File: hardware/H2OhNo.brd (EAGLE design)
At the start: 43.2 x 43.2 mm, 15 parts, among them U2 Tiny85-20-SMT

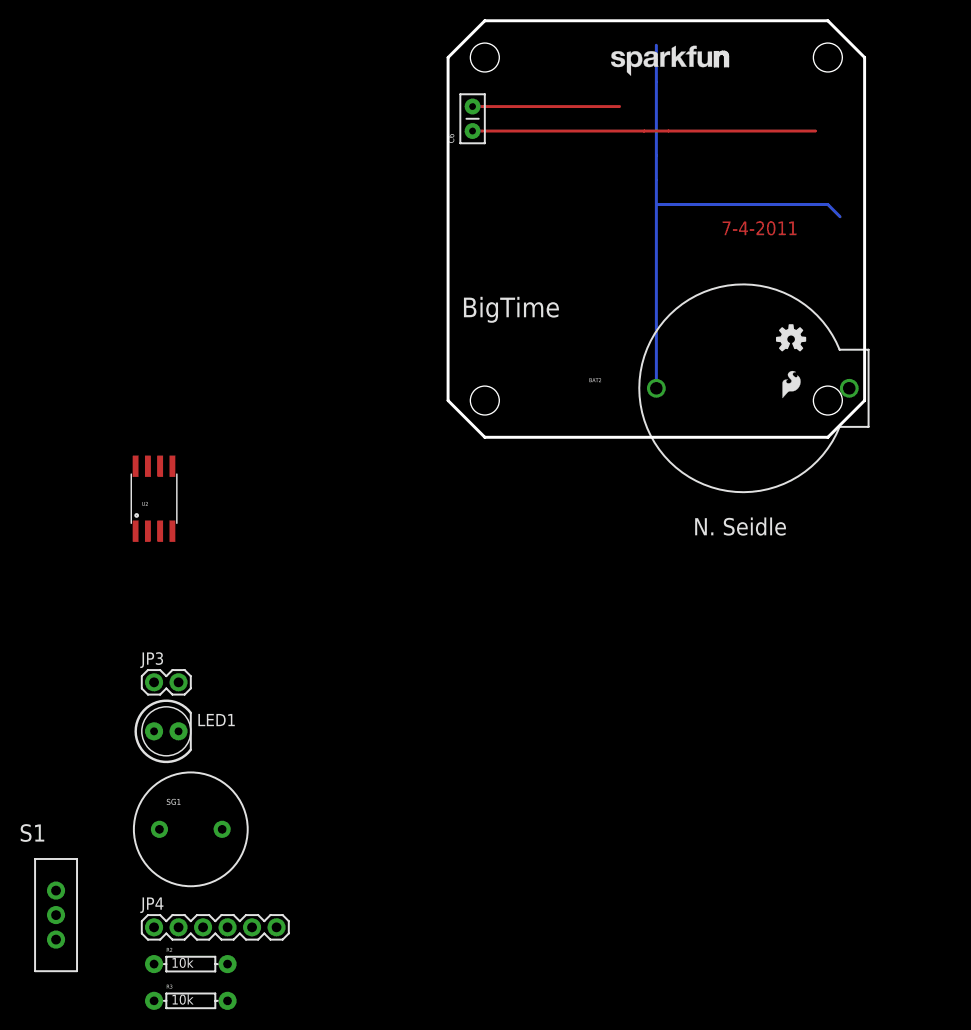
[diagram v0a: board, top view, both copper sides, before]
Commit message: Added version #. Fixed file naming. Removed 10k on RES.
Fixed footprint on CR2032 as well.
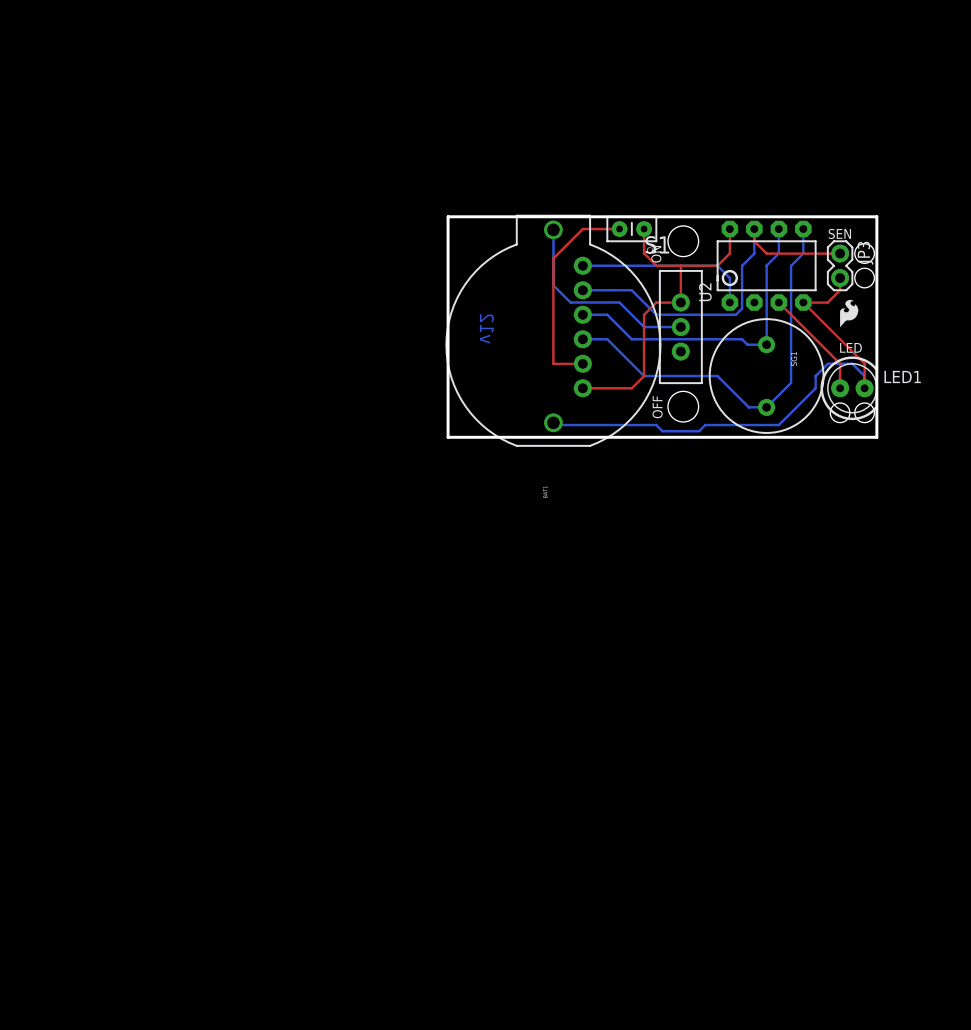
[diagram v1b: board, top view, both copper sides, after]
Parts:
- removed BAT2: (no value), Testing:BATTCOM_20MM_PTH
- removed R2, R3: 10k, SparkFun:AXIAL-0.3
- removed U$3: LOGO-SFENEW, SparkFun:SFE-NEW-WEBLOGO
- added BAT1: (no value), SparkFun-Electromechanical:BATTCOM_20MM_PTH
- U2: value Tiny85-20-SMT -> TINY85-20-DIP; device SparkFun-DigitalIC:SO08-EIAJ -> SparkFun-DigitalIC:DIP08
- moved S1 88.9 mm to (24.1, 11.4)
- moved JP3 83.9 mm to (40.6, 19.1), turned to 270 degrees
- moved JP4 81.7 mm to (14.0, 17.8), flipped to the bottom, turned to 270 degrees
- moved LED1 79.5 mm to (41.9, 5.08)
- moved SG1 76.0 mm to (33.0, 6.35), turned to 270 degrees
- moved U2 67.9 mm to (33.0, 17.8)
- moved U$5 34.3 mm to (4.95, 5.33), flipped to the bottom, turned to 90 degrees
- moved C6 20.5 mm to (20.3, 21.6), turned to 180 degrees
- moved U$4 15.3 mm to (20.3, 11.4), flipped to the bottom, turned to 90 degrees
- moved U$1 9.48 mm to (40.6, 11.4)
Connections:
- removed net N$5: LED1.K, R3.P$2
- net D1: now also SG1.-; no longer LED1.A
- net D4: now also LED1.A
- net GND: now also BAT1.2, LED1.K; no longer BAT2.2, R3.P$1, SG1.-
- net N$1: now also BAT1.1; no longer BAT2.1
- net RESET: no longer R2.P$1
- net VCC: no longer R2.P$2
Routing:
- net D0: track 0.00 -> 42.0 mm
- net D2: track 0.00 -> 37.3 mm
- net D1: track 0.00 -> 32.9 mm
- net N$1: track 0.00 -> 20.8 mm
- net RESET: track 0.00 -> 18.3 mm
- net D4: track 0.00 -> 11.5 mm
- net GND: track 70.4 -> 77.0 mm, vias 1 -> 0
- net VCC: track 35.6 -> 36.4 mm
- added copper zone on layer 1, net GND
- added copper zone on layer 16, net GND
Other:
- board size 43.2 x 43.2 mm -> 44.5 x 22.9 mm
- board text added: "H2OhNo!"
- board text added: "ISP"
- board text added: "LED"
- board text added: "OFF"
- board text added: "ON"
- board text added: "RST"
- board text added: "SEN"
- board text added: "VCC"
- board text added: "v12"
- board text removed: "7-4-2011"
- board text removed: "BLK"
- board text removed: "BigTime"
- board text removed: "Built on:"
- board text removed: "FTDI"
- board text removed: "GRN"

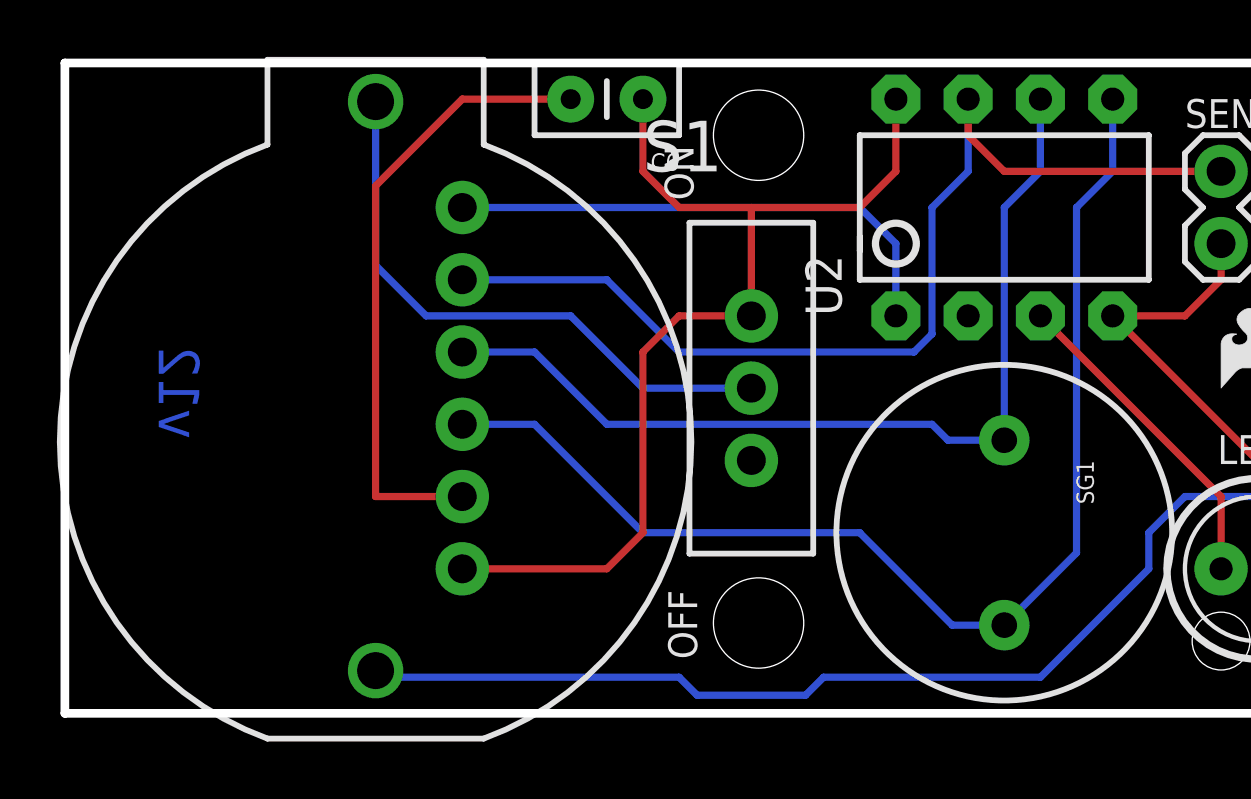
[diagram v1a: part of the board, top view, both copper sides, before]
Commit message: Modified 6-pin SIP header for FTDI compatibility
It's not serial, but you should be able to bit-bang serial out the
MOSI/MISO lines and use an FTDI on the programming header. Good for
debugging.
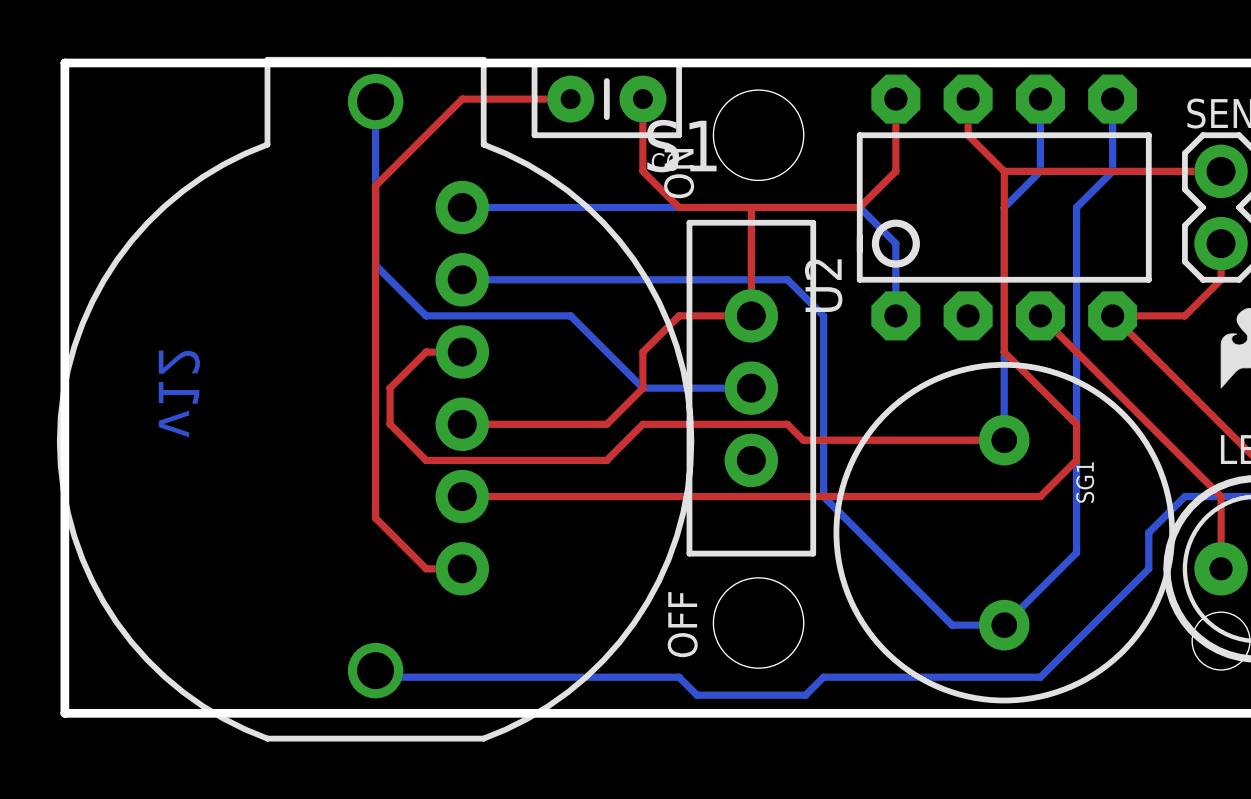
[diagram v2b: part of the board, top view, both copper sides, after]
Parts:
- JP3: value Sense -> Water Sensor
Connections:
- net D0: now also JP4.2; no longer JP4.4
- net D2: now also JP4.5; no longer JP4.2
- net GND: now also JP4.6; no longer JP4.5
- net VCC: now also JP4.4; no longer JP4.6
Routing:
- net D1: track 32.9 -> 39.7 mm
- net D2: track 37.3 -> 44.0 mm
- net D0: track 42.0 -> 47.9 mm
- net VCC: track 36.4 -> 31.3 mm
- net GND: track 77.0 -> 78.5 mm
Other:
- board text added: "GND"
- board text removed: "VCC"
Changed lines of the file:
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@@
 <layer number="106" name="bPlate" color="7" fill="1" visible="no" active="yes"/>
 <layer number="107" name="Crop" color="7" fill="1" visible="no" active="yes"/>
-<layer number="108" name="tplace-old" color="10" fill="1" visible="yes" active="yes"/>
-<layer number="109" name="ref-old" color="11" fill="1" visible="yes" active="yes"/>
+<layer number="108" name="tplace-old" color="10" fill="1" visible="no" active="yes"/>
+<layer number="109" name="ref-old" color="11" fill="1" visible="no" active="yes"/>
 <layer number="116" name="Patch_BOT" color="9" fill="4" visible="no" active="yes"/>
 <layer number="121" name="_tsilk" color="7" fill="1" visible="no" active="yes"/>
@@
 <wire x1="44.45" y1="22.86" x2="0" y2="22.86" width="0.3048" layer="20"/>
 <text x="0.635" y="5.715" size="2.032" layer="22" font="vector" ratio="15" rot="MR90">H2OhNo!</text>
-<text x="3.302" y="9.652" size="1.4224" layer="16" font="vector" ratio="15" rot="SMR90">v12</text>
+<text x="3.302" y="9.652" size="1.4224" layer="16" font="vector" ratio="20" rot="SMR90">v12</text>
 <text x="25.4" y="-10.16" size="1.778" layer="48" font="vector" ratio="15">N. Seidle</text>
 <text x="11.43" y="16.51" size="1.016" layer="22" font="vector" ratio="15" rot="MR90">RST</text>
-<text x="11.43" y="3.81" size="1.016" layer="22" font="vector" ratio="15" rot="MR90">VCC</text>
+<text x="11.43" y="3.81" size="1.016" layer="22" font="vector" ratio="15" rot="MR90">GND</text>
 <text x="10.033" y="9.906" size="1.016" layer="22" font="vector" ratio="15" rot="MR90">ISP</text>
 <hole x="24.384" y="20.32" drill="3.175"/>
@@
 <attribute name="VALUE" value="TINY85-20-DIP" x="33.02" y="17.78" size="1.778" layer="27" font="vector" ratio="15" display="off"/>
 </element>
-<element name="JP3" library="SparkFun-Connectors" package="1X02" value="Sense" x="40.64" y="19.05" rot="R270"/>
+<element name="JP3" library="SparkFun-Connectors" package="1X02" value="Water Sensor" x="40.64" y="19.05" rot="R270"/>
 <element name="LED1" library="SparkFun-LED" package="LED5MM" value="" x="41.91" y="5.08"/>
 <element name="SG1" library="SparkFun-Electromechanical" package="BUZZER-12MM" value="BUZZERPTH" x="33.02" y="6.35" rot="R270"/>
@@
 <signal name="GND">
 <contactref element="C6" pad="2"/>
-<contactref element="JP4" pad="5"/>
 <contactref element="U2" pad="4"/>
 <contactref element="JP3" pad="2"/>
@@
 <wire x1="40.64" y1="15.24" x2="40.64" y2="16.51" width="0.254" layer="1"/>
 <wire x1="17.78" y1="21.59" x2="13.97" y2="21.59" width="0.254" layer="1"/>
-<wire x1="13.97" y1="7.62" x2="10.922" y2="7.62" width="0.254" layer="1"/>
 <wire x1="43.18" y1="5.08" x2="43.18" y2="6.35" width="0.254" layer="16"/>
 <wire x1="43.18" y1="6.35" x2="41.91" y2="7.62" width="0.254" layer="16"/>
@@
 <wire x1="38.1" y1="5.08" x2="34.29" y2="1.27" width="0.254" layer="16"/>
 <wire x1="43.18" y1="7.62" x2="43.18" y2="5.08" width="0.254" layer="1"/>
-<wire x1="10.922" y1="7.62" x2="10.922" y2="18.542" width="0.254" layer="1"/>
+<wire x1="10.922" y1="6.858" x2="10.922" y2="18.542" width="0.254" layer="1"/>
 <wire x1="10.922" y1="18.542" x2="13.97" y2="21.59" width="0.254" layer="1"/>
 <wire x1="34.29" y1="1.27" x2="26.67" y2="1.27" width="0.254" layer="16"/>
@@
 </polygon>
 <contactref element="BAT1" pad="2"/>
+<contactref element="JP4" pad="6"/>
+<wire x1="10.922" y1="6.858" x2="12.7" y2="5.08" width="0.254" layer="1"/>
+<wire x1="12.7" y1="5.08" x2="13.97" y2="5.08" width="0.254" layer="1"/>
 </signal>
 <signal name="VCC">
 <contactref element="C6" pad="1"/>
-<contactref element="JP4" pad="6"/>
 <contactref element="U2" pad="8"/>
 <contactref element="S1" pad="1"/>
-<wire x1="20.32" y1="12.7" x2="20.32" y2="6.35" width="0.254" layer="1"/>
-<wire x1="20.32" y1="6.35" x2="19.05" y2="5.08" width="0.254" layer="1"/>
-<wire x1="19.05" y1="5.08" x2="13.97" y2="5.08" width="0.254" layer="1"/>
 <wire x1="24.13" y1="17.78" x2="27.94" y2="17.78" width="0.254" layer="1"/>
 <wire x1="24.13" y1="13.97" x2="24.13" y2="17.78" width="0.254" layer="1"/>
@@
 <wire x1="27.94" y1="17.78" x2="29.21" y2="19.05" width="0.254" layer="1"/>
 <wire x1="29.21" y1="19.05" x2="29.21" y2="21.59" width="0.254" layer="1"/>
+<contactref element="JP4" pad="4"/>
+<wire x1="13.97" y1="10.16" x2="19.05" y2="10.16" width="0.254" layer="1"/>
+<wire x1="19.05" y1="10.16" x2="20.32" y2="11.43" width="0.254" layer="1"/>
+<wire x1="20.32" y1="11.43" x2="20.32" y2="12.7" width="0.254" layer="1"/>
 </signal>
 <signal name="RESET">
@@
 </signal>
 <signal name="D0">
-<contactref element="JP4" pad="4"/>
 <contactref element="U2" pad="5"/>
 <contactref element="SG1" pad="+"/>
@@
 <wire x1="35.56" y1="5.64" x2="33.02" y2="3.1" width="0.254" layer="16"/>
 <wire x1="33.02" y1="3.1" x2="31.19" y2="3.1" width="0.254" layer="16"/>
-<wire x1="31.19" y1="3.1" x2="27.94" y2="6.35" width="0.254" layer="16"/>
-<wire x1="27.94" y1="6.35" x2="20.32" y2="6.35" width="0.254" layer="16"/>
-<wire x1="20.32" y1="6.35" x2="16.51" y2="10.16" width="0.254" layer="16"/>
-<wire x1="16.51" y1="10.16" x2="13.97" y2="10.16" width="0.254" layer="16"/>
+<wire x1="31.19" y1="3.1" x2="26.67" y2="7.62" width="0.254" layer="16"/>
+<contactref element="JP4" pad="2"/>
+<wire x1="13.97" y1="15.24" x2="25.4" y2="15.24" width="0.254" layer="16"/>
+<wire x1="25.4" y1="15.24" x2="26.67" y2="13.97" width="0.254" layer="16"/>
+<wire x1="26.67" y1="13.97" x2="26.67" y2="7.62" width="0.254" layer="16"/>
 </signal>
 <signal name="D1">
-<contactref element="JP4" pad="3"/>
 <contactref element="U2" pad="6"/>
 <contactref element="SG1" pad="-"/>
-<wire x1="13.97" y1="12.7" x2="16.51" y2="12.7" width="0.254" layer="16"/>
-<wire x1="16.51" y1="12.7" x2="19.05" y2="10.16" width="0.254" layer="16"/>
-<wire x1="33.02" y1="9.6" x2="31.04" y2="9.6" width="0.254" layer="16"/>
-<wire x1="31.04" y1="9.6" x2="30.48" y2="10.16" width="0.254" layer="16"/>
-<wire x1="30.48" y1="10.16" x2="19.05" y2="10.16" width="0.254" layer="16"/>
 <wire x1="34.29" y1="21.59" x2="34.29" y2="19.05" width="0.254" layer="16"/>
 <wire x1="34.29" y1="19.05" x2="33.02" y2="17.78" width="0.254" layer="16"/>
 <wire x1="33.02" y1="17.78" x2="33.02" y2="9.6" width="0.254" layer="16"/>
+<contactref element="JP4" pad="3"/>
+<wire x1="33.02" y1="9.6" x2="25.96" y2="9.6" width="0.254" layer="1"/>
+<wire x1="25.96" y1="9.6" x2="25.4" y2="10.16" width="0.254" layer="1"/>
+<wire x1="25.4" y1="10.16" x2="20.32" y2="10.16" width="0.254" layer="1"/>
+<wire x1="20.32" y1="10.16" x2="19.05" y2="8.89" width="0.254" layer="1"/>
+<wire x1="19.05" y1="8.89" x2="12.7" y2="8.89" width="0.254" layer="1"/>
+<wire x1="12.7" y1="8.89" x2="11.43" y2="10.16" width="0.254" layer="1"/>
+<wire x1="11.43" y1="10.16" x2="11.43" y2="11.43" width="0.254" layer="1"/>
+<wire x1="11.43" y1="11.43" x2="12.7" y2="12.7" width="0.254" layer="1"/>
+<wire x1="12.7" y1="12.7" x2="13.97" y2="12.7" width="0.254" layer="1"/>
 </signal>
 <signal name="D2">
-<contactref element="JP4" pad="2"/>
 <contactref element="U2" pad="7"/>
 <contactref element="JP3" pad="1"/>
-<wire x1="13.97" y1="15.24" x2="19.05" y2="15.24" width="0.254" layer="16"/>
-<wire x1="19.05" y1="15.24" x2="21.59" y2="12.7" width="0.254" layer="16"/>
-<wire x1="21.59" y1="12.7" x2="29.845" y2="12.7" width="0.254" layer="16"/>
-<wire x1="29.845" y1="12.7" x2="30.48" y2="13.335" width="0.254" layer="16"/>
 <wire x1="40.64" y1="19.05" x2="33.02" y2="19.05" width="0.254" layer="1"/>
-<wire x1="30.48" y1="13.335" x2="30.48" y2="17.78" width="0.254" layer="16"/>
-<wire x1="30.48" y1="17.78" x2="31.75" y2="19.05" width="0.254" layer="16"/>
-<wire x1="31.75" y1="19.05" x2="31.75" y2="21.59" width="0.254" layer="16"/>
+<contactref element="JP4" pad="5"/>
+<wire x1="13.97" y1="7.62" x2="34.29" y2="7.62" width="0.254" layer="1"/>
+<wire x1="34.29" y1="7.62" x2="35.56" y2="8.89" width="0.254" layer="1"/>
+<wire x1="35.56" y1="8.89" x2="35.56" y2="10.16" width="0.254" layer="1"/>
+<wire x1="35.56" y1="10.16" x2="33.02" y2="12.7" width="0.254" layer="1"/>
+<wire x1="33.02" y1="12.7" x2="33.02" y2="19.05" width="0.254" layer="1"/>
 <wire x1="33.02" y1="19.05" x2="31.75" y2="20.32" width="0.254" layer="1"/>
 <wire x1="31.75" y1="20.32" x2="31.75" y2="21.59" width="0.254" layer="1"/>
